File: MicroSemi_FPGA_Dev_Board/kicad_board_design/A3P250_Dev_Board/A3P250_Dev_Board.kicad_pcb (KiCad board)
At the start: 4 copper layers, 46.7 x 46.7 mm, 50 parts, among them J1 Conn_01x20, J2 Conn_01x20, J3 Conn_01x20, J4 Conn_01x20, U1 A3P250, U2 LTC3561A, U3 LT1962-3.3, X1 ASE-25MHz

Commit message: Routed, fixed labels, added test points.
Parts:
- added +5V: +5V, TestPoint:TestPoint_THTPad_1.5x1.5mm_Drill0.7mm, F.Cu at (107.1, 92.9)
- added CLK: VCCIO, TestPoint:TestPoint_THTPad_1.5x1.5mm_Drill0.7mm, F.Cu at (112.3, 111.6)
- added GND: GND, TestPoint:TestPoint_THTPad_1.5x1.5mm_Drill0.7mm, F.Cu at (107.0, 96.5)
- added J1: Conn_01x20, Connector_PinHeader_2.00mm:PinHeader_1x20_P2.00mm_Vertical, F.Cu at (104.9, 86.3)
- added J2: Conn_01x20, Connector_PinHeader_2.00mm:PinHeader_1x20_P2.00mm_Vertical, F.Cu at (146.9, 90.3)
- added J3: Conn_01x20, Connector_PinHeader_2.00mm:PinHeader_1x20_P2.00mm_Vertical, F.Cu at (142.9, 132.3)
- added VCCIO: VCCIO, TestPoint:TestPoint_THTPad_1.5x1.5mm_Drill0.7mm, F.Cu at (136.0, 101.8)
- added VCore: 1.5V Core, TestPoint:TestPoint_THTPad_1.5x1.5mm_Drill0.7mm, F.Cu at (110.8, 121.8)
- added VPLL: 1.5V PLL, TestPoint:TestPoint_THTPad_1.5x1.5mm_Drill0.7mm, F.Cu at (116.6, 101.3)
- moved R7 5.81 mm to (119.7, 121.6)
- moved J4 2.00 mm to (100.9, 128.3)
- moved J4 2.00 mm to (102.9, 128.3)
- moved C28 0.23 mm to (117.7, 117.3)
- moved C29 0.23 mm to (117.7, 116.1)
- moved C12 0.10 mm to (117.6, 114.5)
- moved C13 0.10 mm to (117.6, 113.3)
- moved C14 0.10 mm to (117.6, 118.7)
- moved C15 0.10 mm to (117.6, 120.0)
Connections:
- U1 pad 100: GND -> Net-(C22-Pad1)
- U1 pad 24: GND -> VCCIB3
- U1 pad 50: GND -> Net-(C26-Pad1)
- U1 pad 74: GND -> Net-(C24-Pad1)
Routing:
- net VCCIB3: track 100.1 -> 129.8 mm, vias 4 -> 5
- net Net-(J4-Pad1): track 0.00 -> 23.6 mm
- net Net-(J4-Pad2): track 1.56 -> 22.2 mm
- net Net-(J4-Pad3): track 1.10 -> 21.7 mm, vias 1 -> 0
- net Net-(J4-Pad5): track 0.00 -> 20.3 mm, vias 0 -> 1
- net Net-(C22-Pad1): track 27.0 -> 42.6 mm, vias 2 -> 3
- net Net-(C26-Pad1): track 14.7 -> 28.9 mm, vias 2 -> 3
- net Net-(C24-Pad1): track 23.9 -> 34.4 mm, vias 2 -> 3
- net Net-(J1-Pad2): track 26.5 -> 30.4 mm
- net Net-(J1-Pad1): track 28.2 -> 32.1 mm
- net Net-(J4-Pad7): track 18.2 -> 22.2 mm, vias 0 -> 1
- net +5V: track 53.4 -> 56.0 mm
- net Net-(J1-Pad4): track 25.7 -> 27.9 mm
- net TMS: track 15.0 -> 17.0 mm
- net VPUMP: track 12.4 -> 14.4 mm
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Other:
- board size 46.7 x 46.7 mm -> 46 x 46 mm
- board text added: "+5V GND P98 P2 P4 P5 P6 P7 P8 P10 P11 P13 P15 P16 VCCIO P19 P20 P21 P22 P23"
- board text added: "P26"
- board text added: "P27 P28 P29 P30 P31 P32 P33 P34 P35 P36 P39 P40 P41 P42 P43 P44 P45 TCK"
- board text added: "P73 P72 P71 P70 P69 P66 P65 P64 P63 P62 P61 P60 P59 P58 P57 VJTAG TRST TDO VPUMP TMS"
- board text added: "P76"
- board text added: "P96 P95 P94 P93 P92 P91 P90 P87 P86 P85 P84 P83 P82 P81 P80 P79 P78 P77"
- board text added: "P97"
- board text added: "TDI"
- board text removed: "+5V GND 0RSB0 118UDB3 117UDB3 117VDB3 116UDB3 116VDB3 112P 109PDB3 109NDB3 108NDB3 108PPB3 107PSB3 VCCIB3 105PSB3 100PDB3 100NDB3 98PDB3 98NDB3"
- board text removed: "41PDB1 41NDB1 42PSB1 43PDB1 43NDB1 VCCIB1 48PDB1 48NDB1 50NDB1 50PDB1 52PDB1 52NDB1 58UDB1 58VDB1 60USB1 VJTAG TRST TDO VPUMP TMS"
- board text removed: "TDI TCK 61RSB2 62RSB2 63RSB2 71RSB2 74RSB2 77RSB2 VCCIB2 84RSB2 85RSB2 86RSB2 88RSB2 90RSB2 91RSB2 92RSB2 93RSB2 95RSB2"

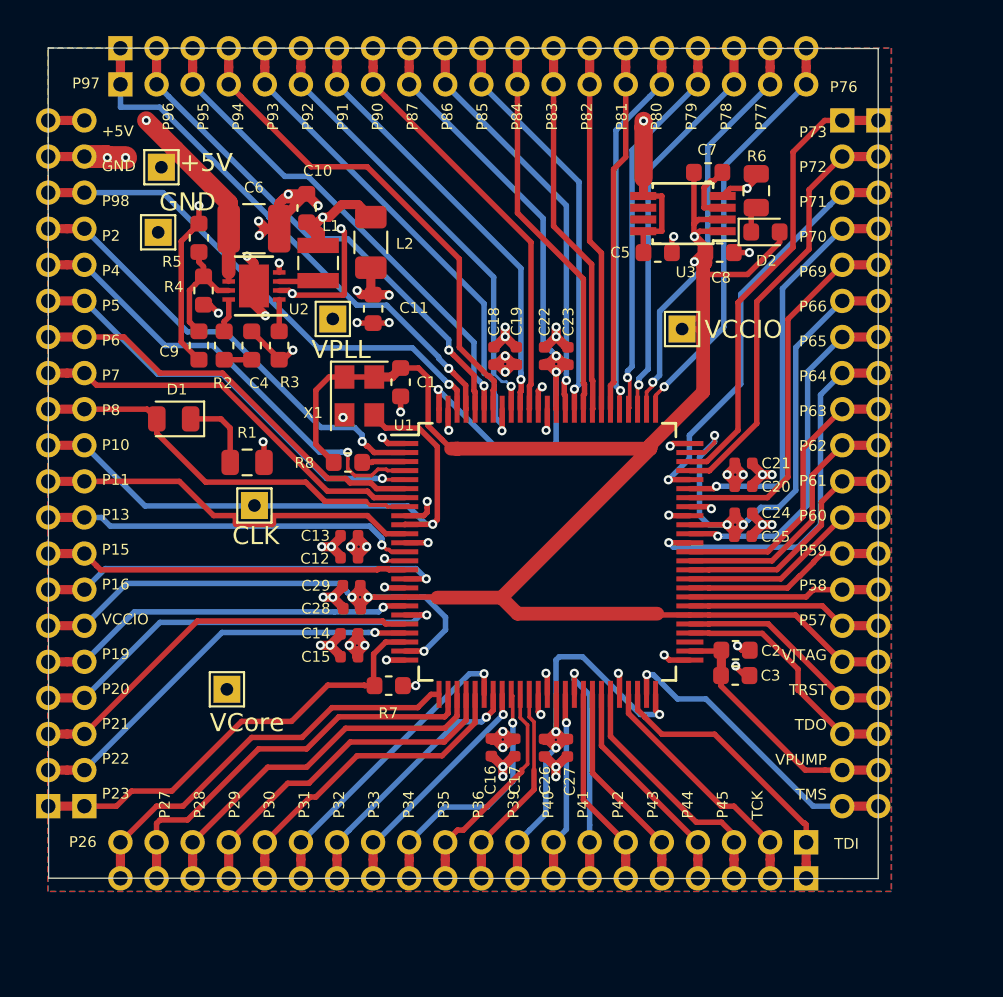
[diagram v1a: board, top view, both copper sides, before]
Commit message: Add solder paste layer.
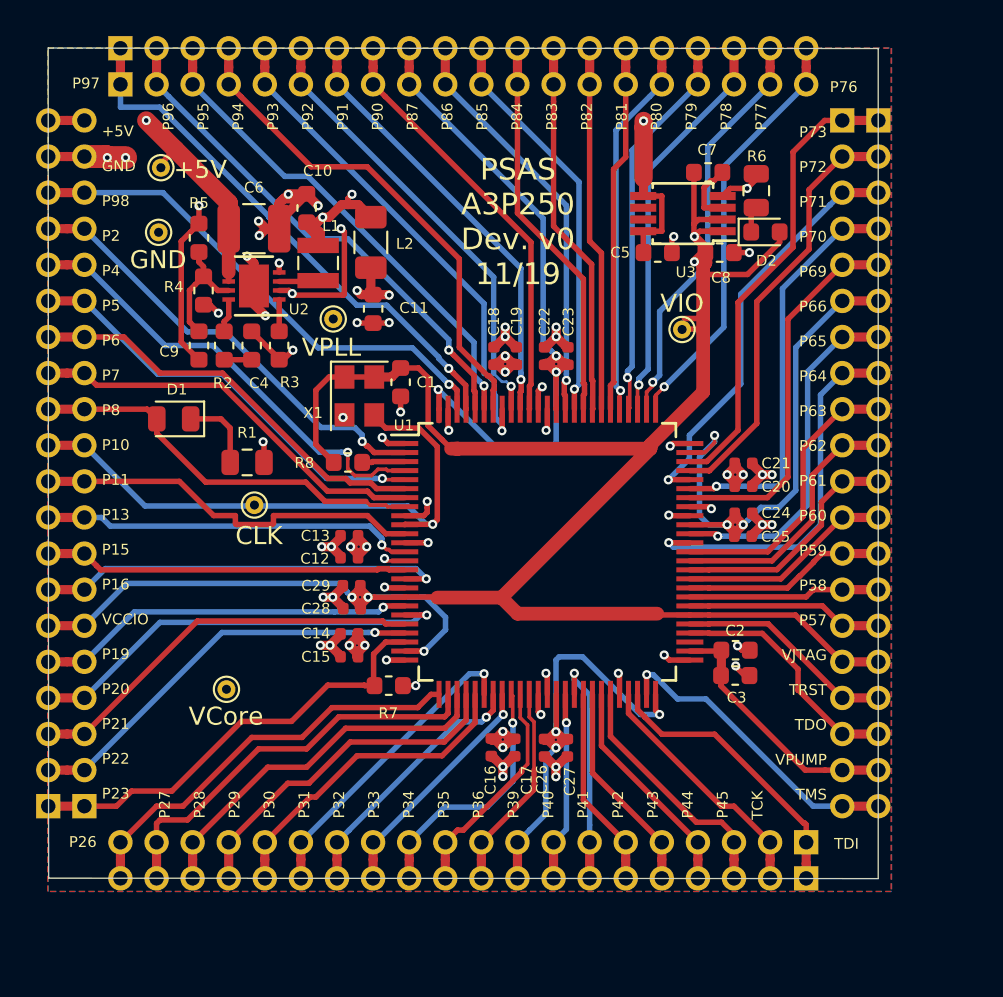
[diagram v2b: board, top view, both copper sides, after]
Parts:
- removed the +5V at (107.1, 92.9)
- removed the CLK at (112.3, 111.6)
- removed the GND at (107.0, 96.5)
- removed VCCIO: VCCIO, TestPoint:TestPoint_THTPad_1.5x1.5mm_Drill0.7mm
- removed the VCore at (110.8, 121.8)
- removed the VPLL at (116.6, 101.3)
- added +5V: +5V, TestPoint:TestPoint_THTPad_D1.0mm_Drill0.5mm, F.Cu at (107.1, 92.9)
- added CLK: VCCIO, TestPoint:TestPoint_THTPad_D1.0mm_Drill0.5mm, F.Cu at (112.3, 111.6)
- added GND: GND, TestPoint:TestPoint_THTPad_D1.0mm_Drill0.5mm, F.Cu at (107.0, 96.5)
- added VCore: 1.5V Core, TestPoint:TestPoint_THTPad_D1.0mm_Drill0.5mm, F.Cu at (110.7, 121.8)
- added VIO: VCCIO, TestPoint:TestPoint_THTPad_D1.0mm_Drill0.5mm, F.Cu at (136.0, 101.9)
- added VPLL: 1.5V PLL, TestPoint:TestPoint_THTPad_D1.0mm_Drill0.5mm, F.Cu at (116.7, 101.3)
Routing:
- net Net-(C10-Pad1): track 46.5 -> 47.2 mm, vias 14 -> 15
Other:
- board text added: "PSAS A3P250 Dev. v0 11/19"
